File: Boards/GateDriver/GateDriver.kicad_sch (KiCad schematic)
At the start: 23 parts, among them J1 Conn_02x08_Counter_Clockwise

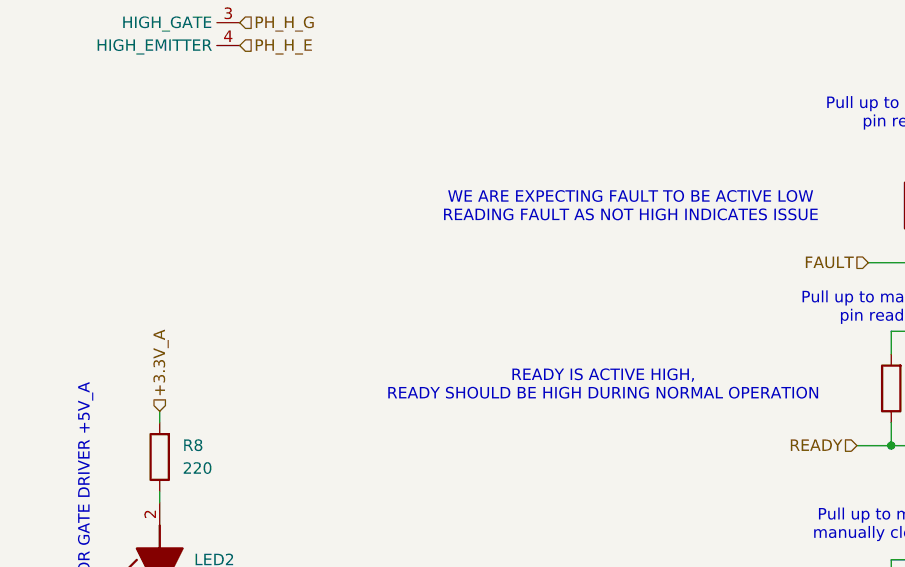
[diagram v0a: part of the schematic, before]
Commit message: fix connector pinout
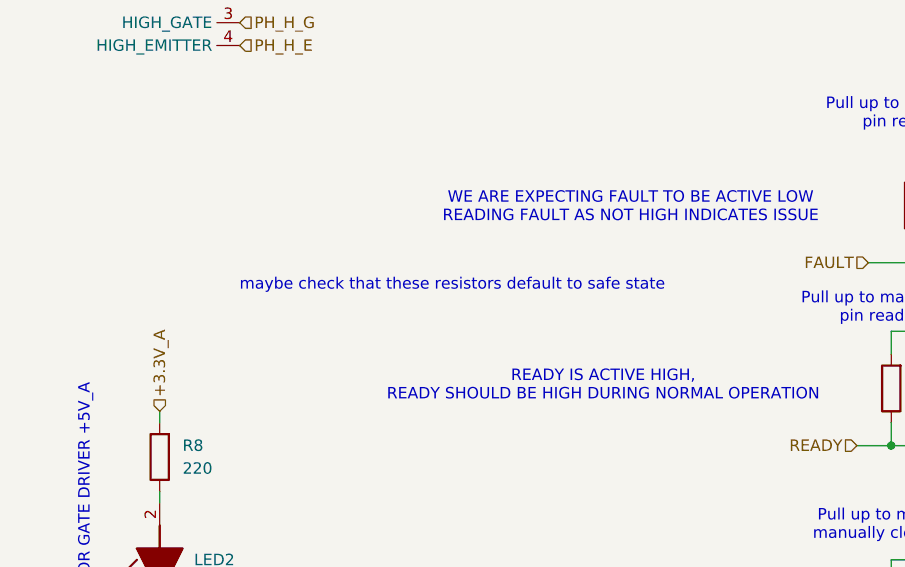
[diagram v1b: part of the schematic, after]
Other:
- note added: "maybe check that these resistors default to safe state"
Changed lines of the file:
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@@
+		)
+	)
+	(text "maybe check that these resistors default to safe state"
+		(exclude_from_sim no)
+		(at 103.632 114.3 0)
+		(effects
+			(font
+				(size 1.27 1.27)
+			)
 		)
 	)
